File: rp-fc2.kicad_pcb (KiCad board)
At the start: 4 copper layers, 45 x 75 mm, 92 parts, among them CN1 20021521-00010T1LF, J1 USB_C_Receptacle_USB2.0_16P, J2 Conn_01x03, J3 Conn_01x05, J4 Conn_01x05, J5 Conn_01x05, J6 OV7670 Breakout, SW1 SW_Push, SW3 SW_Push, U1 RP2350A-QFN60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

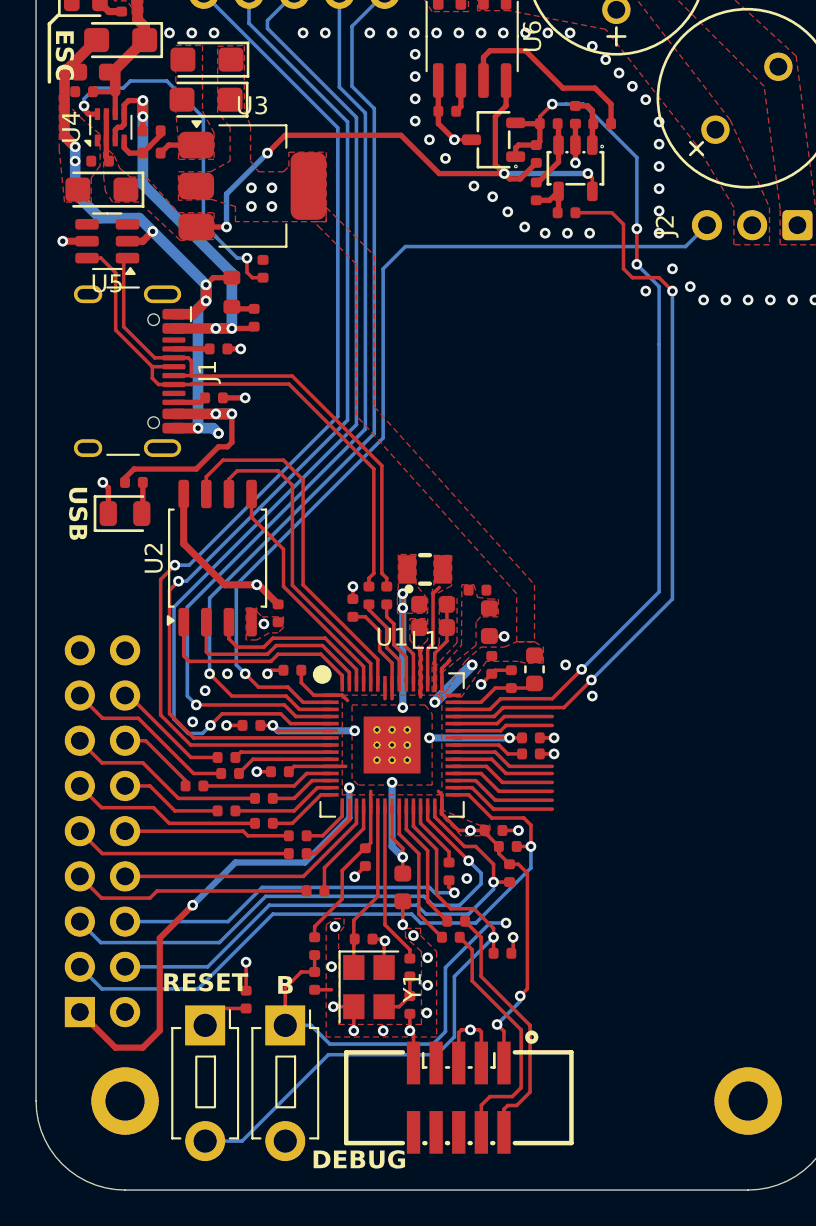
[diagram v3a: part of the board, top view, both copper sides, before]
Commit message: rp2350B -- larger package
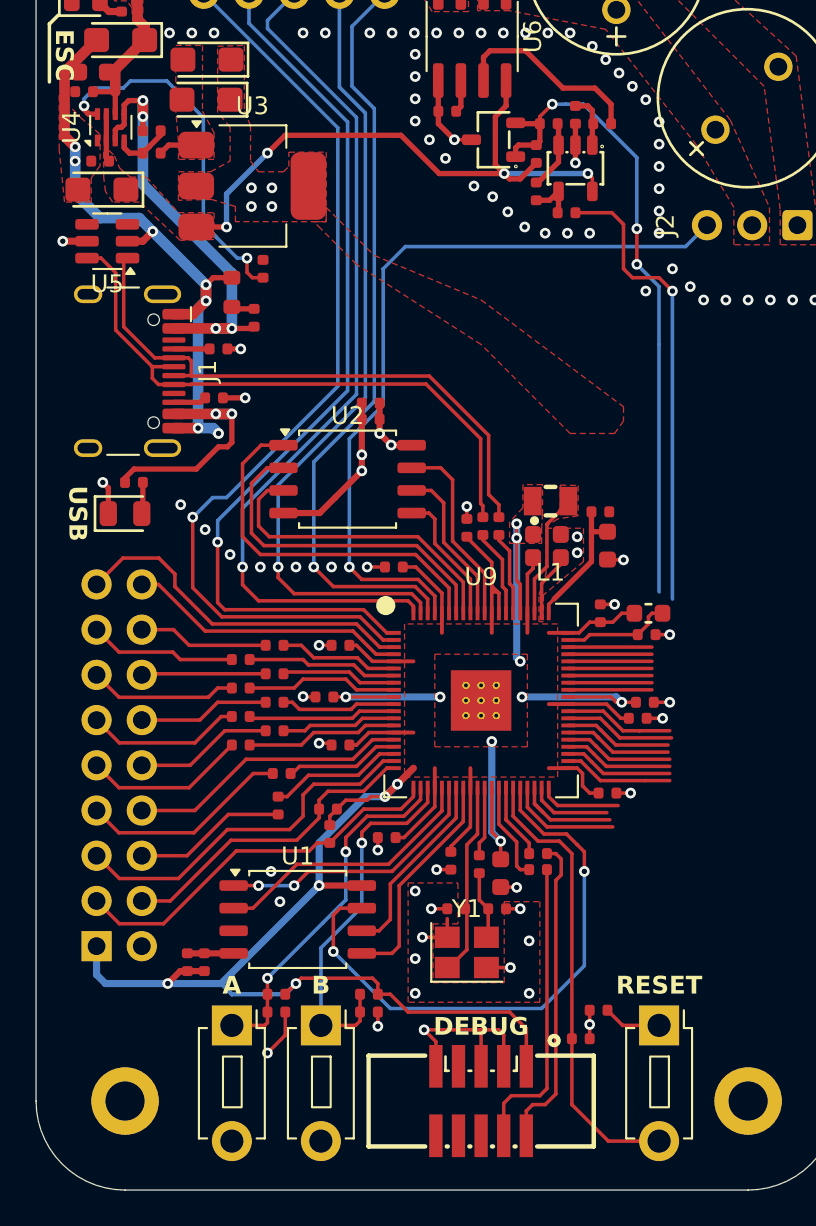
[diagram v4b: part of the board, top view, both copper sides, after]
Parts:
- added C31: 100nF, PCM_JLCPCB:C_0402, F.Cu at (120.1, 115.0)
- added C33: 100nF, PCM_JLCPCB:C_0402, F.Cu at (118.8, 106.7)
- added C34: 100nF, PCM_JLCPCB:C_0402, F.Cu at (131.7, 117.6)
- added C35: 100nF, PCM_JLCPCB:C_0402, F.Cu at (118.7, 140.0)
- added C36: 100nF, PCM_JLCPCB:C_0402, F.Cu at (108.5, 137.2)
- added C37: 100nF, PCM_JLCPCB:C_0402, F.Cu at (109.5, 137.2)
- added R36: 10kΩ, PCM_JLCPCB:R_0402, F.Cu at (118.7, 139.0)
- added SW2: SW_Push, Button_Switch_THT:SW_PUSH_1P1T_6x3.5mm_H4.3_APEM_MJTP1243, F.Cu at (116.0, 140.8)
- added U9: RP2350B-QFN80, RP2350_KiCad:RP2350B_QFN-80_EP_10.573x10.573_Pitch0.4mm, F.Cu at (125.0, 122.5)
- U1: value RP2350A-QFN60 -> W25Q128JVS; footprint RP2350_KiCad:RP2350A_QFN-60_EP_7.75x7.75_Pitch0.4mm -> Package_SO:SOIC-8_5.23x5.23mm_P1.27mm
- moved SW1 25.5 mm to (135.0, 140.8)
- moved C5 22.1 mm to (134.2, 122.6), turned to 0 degrees
- moved R4 19.8 mm to (131.6, 139.9), turned to 0 degrees
- moved C15 12.9 mm to (118.8, 105.8), turned to 180 degrees
- moved C4 11.8 mm to (116.2, 122.3), turned to 180 degrees
- moved U1 11.1 mm to (114.7, 134.8)
- moved R34 10.8 mm to (116.4, 128.6), turned to 180 degrees
- moved R33 10.3 mm to (113.6, 128.4)
- moved R35 10.0 mm to (116.5, 130.0), turned to -90 degrees
- moved C9 8.73 mm to (133.8, 123.5), turned to 0 degrees
- moved U2 8.54 mm to (117.5, 110.1), turned to 0 degrees
- moved R1 8.18 mm to (131.7, 111.9)
- moved L1 8.03 mm to (128.9, 111.3)
- moved C7 8.00 mm to (134.3, 118.8), turned to 0 degrees
- moved C1 7.91 mm to (132.1, 113.8)
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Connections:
- C1 pad 1: Net-(U1-VREG_AVDD) -> Net-(U9-VREG_AVDD)
- C18 pad 1: Net-(U1-RUN) -> Net-(U9-RUN)
- L1 pad 1: Net-(U1-VREG_LX) -> Net-(U9-VREG_LX)
- R1 pad 2: Net-(U1-VREG_AVDD) -> Net-(U9-VREG_AVDD)
- R2 pad 1: Net-(U1-USB_DP) -> Net-(U9-USB_DP)
- R23 pad 1: Net-(U1-GPIO6) -> Net-(U9-GPIO8)
- R25 pad 1: Net-(U1-GPIO7) -> Net-(U9-GPIO9)
- R26 pad 1: Net-(U1-GPIO8) -> Net-(U9-GPIO10)
- R27 pad 1: Net-(U1-GPIO9) -> Net-(U9-GPIO11)
- R28 pad 1: Net-(U1-GPIO10) -> Net-(U9-GPIO12)
- R29 pad 1: Net-(U1-GPIO11) -> Net-(U9-GPIO13)
- R3 pad 1: Net-(U1-USB_DM) -> Net-(U9-USB_DM)
- R30 pad 1: Net-(U1-GPIO12) -> Net-(U9-GPIO14)
- R31 pad 1: Net-(U1-GPIO13) -> Net-(U9-GPIO15)
- R32 pad 1: Net-(U1-GPIO15) -> Net-(U9-GPIO17)
- R33 pad 1: Net-(U1-GPIO16) -> Net-(U9-GPIO18)
- R6 pad 2: Net-(U1-SWCLK) -> Net-(U9-SWCLK)
- R7 pad 2: Net-(U1-SWDIO) -> Net-(U9-SWDIO)
- SW1 pad 2: Net-(U1-RUN) -> Net-(U9-RUN)
- U1 pad 1: +3V3 -> SPI1_CS1
- U1 pad 2: CH1 -> SPI1_MISO
- U1 pad 3: CH6 -> unconnected-(U1-IO2-Pad3)
- U1 pad 4: CH5 -> GND
- U1 pad 5: CH4 -> SPI1_MOSI
- U1 pad 6: +1V1 -> SPI1_SCK
- U1 pad 7: CH3 -> FLASH2_RESET
- U1 pad 8: CH2 -> +3V3
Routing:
- net Net-(U1-RUN): track 33.8 -> 0.00 mm, vias 1 -> 0
- net FLASH2_RESET: track 0.00 -> 32.5 mm, vias 0 -> 2
- net Net-(U9-RUN): track 0.00 -> 25.6 mm
- net +3V3: track 88.2 -> 111.7 mm, vias 12 -> 11
- net USR_SW2: track 0.00 -> 20.8 mm, vias 0 -> 1
- net CAMERA_RST: track 0.00 -> 19.8 mm
- net GND: track 81.9 -> 98.5 mm, vias 93 -> 100
- net CAMERA_PWDN: track 0.00 -> 15.8 mm
- net SIO_C: track 37.4 -> 21.8 mm, vias 1 -> 0
- net SPI1_MISO: track 0.00 -> 15.3 mm
- net SPI1_CS1: track 0.00 -> 15.3 mm, vias 0 -> 2
- net I_COND: track 41.1 -> 26.0 mm, vias 2 -> 1
- net I_COND_2_5: track 51.0 -> 36.7 mm, vias 4 -> 3
- net SPI1_MOSI: track 0.00 -> 12.7 mm
- net SIO_D: track 30.2 -> 17.8 mm, vias 1 -> 0
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- added copper zone on F.Cu, net Net-(U9-VREG_LX)
- removed copper zone on F.Cu, net Net-(U1-VREG_AVDD)
- removed copper zone on F.Cu, net Net-(U1-VREG_LX)
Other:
- board text added: "A"

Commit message: nrf52833-discrete
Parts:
- added AE1: 2.4GHz, PCM_JLCPCB:L_1206, F.Cu at (95.0, 138.6)
- added C38: 100nF, PCM_JLCPCB:C_0402, F.Cu at (138.0, 137.4)
- added C39: 4.7uF, PCM_JLCPCB:C_0603, F.Cu at (132.4, 136.6)
- added C40: 1uF, PCM_JLCPCB:C_0402, F.Cu at (140.8, 140.5)
- added C41: 100nF, PCM_JLCPCB:C_0402, F.Cu at (139.1, 144.8)
- added C42: 1uF, PCM_JLCPCB:C_0402, F.Cu at (139.8, 140.5)
- added C43: 100pF, PCM_JLCPCB:C_0402, F.Cu at (136.8, 147.5)
- added C44: 100nF, PCM_JLCPCB:C_0402, F.Cu at (129.7, 143.4)
- added C45: 1nF, PCM_JLCPCB:C_0402, F.Cu at (130.5, 145.3)
- added C46: 100nF, PCM_JLCPCB:C_0402, F.Cu at (155.7, 144.1)
- added C47: 1pF, PCM_JLCPCB:C_0402, F.Cu at (133.7, 147.2)
- added C48: 1.2pF, PCM_JLCPCB:C_0402, F.Cu at (133.7, 150.9)
- added C49: 15pF, PCM_JLCPCB:C_0402, F.Cu at (139.9, 146.7)
- added C50: 15pF, PCM_JLCPCB:C_0402, F.Cu at (142.0, 146.7)
- added CN2: 20021521-00010T1LF, easyeda2kicad:IDC-SMD_10P-P1.27_X1270WVS-2X05B-6TV01, F.Cu at (114.2, 155.4)
- added D3: H5VUT1B, PCM_JLCPCB:SOT-143-4_L2.9-W1.3-P1.90-LS2.4-BL-1, F.Cu at (163.9, 124.1)
- added J7: U.FL, PCM_JLCPCB:IPEX-SMD_BWIPX-1-001E, F.Cu at (133.2, 154.8)
- added J8: Conn_01x04, Connector_PinHeader_2.54mm:PinHeader_1x04_P2.54mm_Vertical, F.Cu at (170.4, 119.8)
- added L2: 4.7nH,300mA, PCM_JLCPCB:L_0402, F.Cu at (133.2, 149.0)
- added L3: 2.2nH,300mA, PCM_JLCPCB:L_0402, F.Cu at (133.2, 152.4)
- added R37: 10kΩ, PCM_JLCPCB:R_0402, F.Cu at (155.7, 146.0)
- added R38: 10kΩ, PCM_JLCPCB:R_0402, F.Cu at (130.6, 136.4)
- added R39: 10kΩ, PCM_JLCPCB:R_0402, F.Cu at (130.6, 139.2)
- added R40: 10kΩ, PCM_JLCPCB:R_0402, F.Cu at (128.6, 142.0)
- added SW4: SW_Push, Button_Switch_THT:SW_PUSH_1P1T_6x3.5mm_H4.3_APEM_MJTP1243, F.Cu at (156.7, 141.6)
- added U10: nRF52833_QDxx, Package_DFN_QFN:QFN-40-1EP_5x5mm_P0.4mm_EP3.6x3.6mm, F.Cu at (135.0, 142.0)
- added X1: X201632MOB4SI, PCM_JLCPCB:OSC-SMD_4P-L3.2-W2.5-BL, F.Cu at (140.4, 148.9)
- moved SW1 27.8 mm to (109.0, 150.6), turned to 180 degrees
- moved R4 22.1 mm to (111.3, 148.6), turned to 180 degrees
- moved C18 20.2 mm to (111.3, 147.6)
- moved H4 11.2 mm to (145.0, 155.0)
- moved H3 10.0 mm to (105.0, 155.0)
- moved SW2 8.47 mm to (109.0, 145.6), turned to 180 degrees
- moved R36 7.52 mm to (112.4, 143.1), turned to -90 degrees
- moved CN1 7.41 mm to (117.6, 144.6), turned to 90 degrees
- moved C35 6.91 mm to (112.0, 141.7), turned to 180 degrees
- moved R24 5.66 mm to (110.2, 143.6)
- moved H2 5.00 mm to (145.0, 80.0)
- moved C32 4.20 mm to (110.2, 142.6)
- moved SW3 2.06 mm to (109.0, 140.6), turned to 180 degrees
- moved R6 0.95 mm to (127.9, 132.9), turned to 90 degrees
- moved R1 0.72 mm to (131.0, 111.8), turned to -90 degrees
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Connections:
- C18 pad 1: Net-(U9-RUN) -> RP2350_RUN
- CN1 pad 10: unconnected-(CN1-Pad10) -> RP2350_RUN
- SW1 pad 2: Net-(U9-RUN) -> RP2350_RUN
- U9 pad 35: Net-(U9-RUN) -> RP2350_RUN
- U9 pad 37: unconnected-(U9-GPIO29-Pad37) -> NRF_AUX1
- U9 pad 38: unconnected-(U9-GPIO30-Pad38) -> NRF_AUX2
- U9 pad 39: unconnected-(U9-GPIO31-Pad39) -> NRF_AUX3
- U9 pad 40: unconnected-(U9-GPIO32-Pad40) -> SPI0_MISO
- U9 pad 42: unconnected-(U9-GPIO33-Pad42) -> SPI0_CS
- U9 pad 43: unconnected-(U9-GPIO34-Pad43) -> SPIO_SCK
- U9 pad 44: unconnected-(U9-GPIO35-Pad44) -> SPIO_MOSI
- U9 pad 57: unconnected-(U9-GPIO46_ADC6-Pad57) -> I_COND
- U9 pad 58: unconnected-(U9-GPIO47_ADC7-Pad58) -> I_COND_2_5
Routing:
- net +3V3: track 111.7 -> 229.7 mm, vias 11 -> 18
- net RP2350_RUN: track 0.00 -> 45.7 mm, vias 0 -> 2
- net GND: track 98.5 -> 127.2 mm, vias 100 -> 171
- net NRF_SWCLK: track 0.00 -> 28.6 mm
- net NRF_NRESET: track 0.00 -> 28.5 mm, vias 0 -> 2
- net Net-(U9-RUN): track 25.6 -> 0.00 mm
- net NRF_SWDIO: track 0.00 -> 24.3 mm
- net NRF_AUX1: track 0.00 -> 21.4 mm
- net NRF_AUX2: track 0.00 -> 19.9 mm
- net NRF_AUX3: track 0.00 -> 18.2 mm
- net SPIO_MOSI: track 0.00 -> 18.1 mm
- net SPIO_SCK: track 0.00 -> 17.4 mm
- net SPI0_CS: track 0.00 -> 16.6 mm
- net SPI0_MISO: track 0.00 -> 15.1 mm
- net /IO/DEC4_6: track 0.00 -> 12.6 mm, vias 0 -> 2
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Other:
- board size 45 x 75 mm -> 50 x 85 mm
- board text added: "NRF DEBUG"
- board text added: "PI DEBUG"
- board text added: "PI RUN"
- board text removed: "DEBUG"
- board text removed: "RESET"

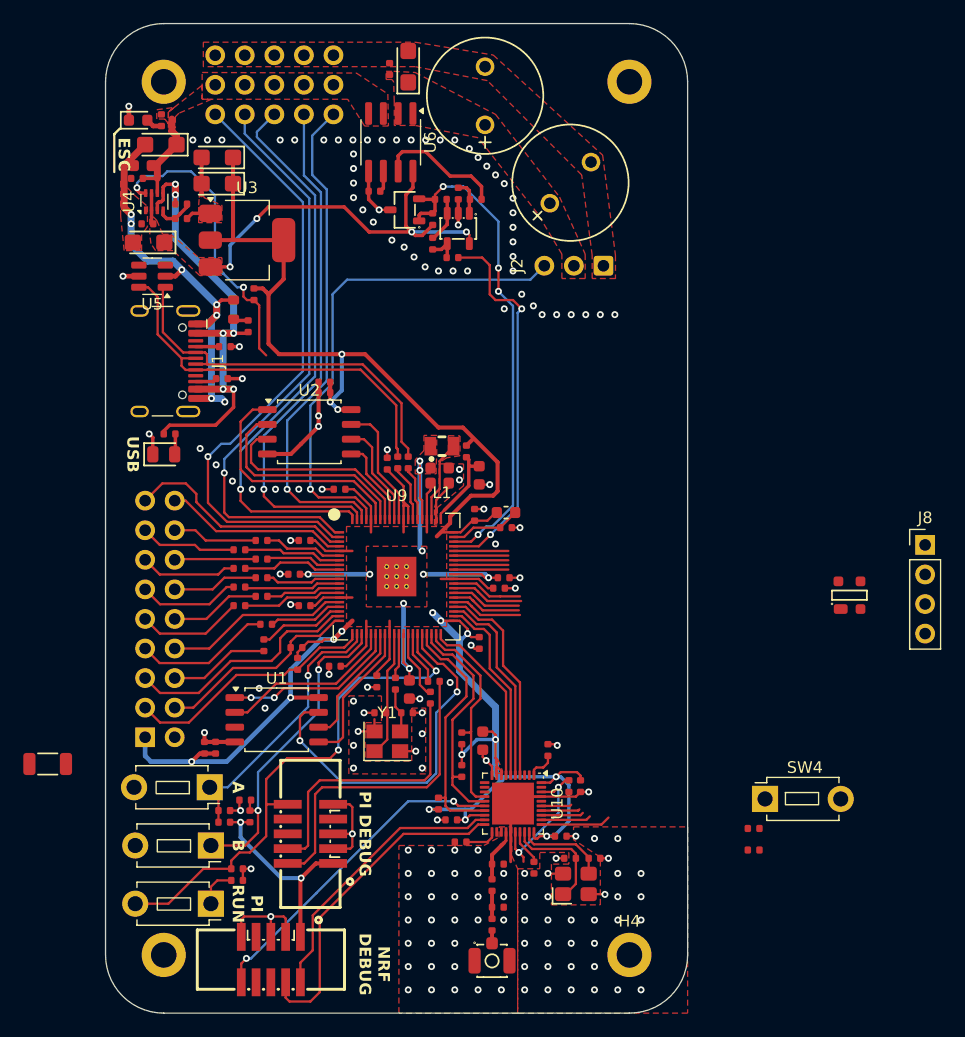
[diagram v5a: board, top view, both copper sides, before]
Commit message: nrf54L BLE module
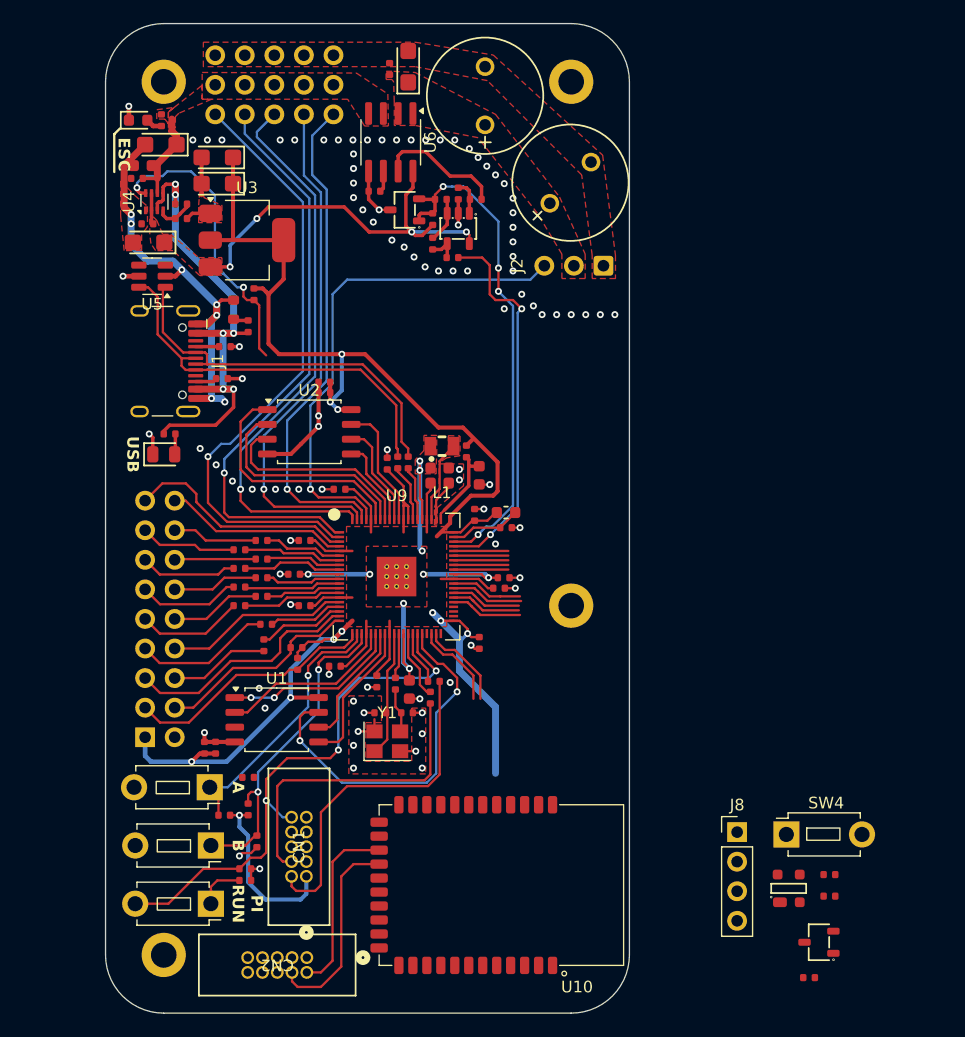
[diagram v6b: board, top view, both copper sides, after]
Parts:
- removed AE1: 2.4GHz, PCM_JLCPCB:L_1206
- removed C38, C41, C44: 100nF, PCM_JLCPCB:C_0402
- removed C39: 4.7uF, PCM_JLCPCB:C_0603
- removed C40, C42: 1uF, PCM_JLCPCB:C_0402
- removed C43: 100pF, PCM_JLCPCB:C_0402
- removed C45: 1nF, PCM_JLCPCB:C_0402
- removed C47: 1pF, PCM_JLCPCB:C_0402
- removed C48: 1.2pF, PCM_JLCPCB:C_0402
- removed C49, C50: 15pF, PCM_JLCPCB:C_0402
- removed J7: U.FL, PCM_JLCPCB:IPEX-SMD_BWIPX-1-001E
- removed L2: 4.7nH,300mA, PCM_JLCPCB:L_0402
- removed L3: 2.2nH,300mA, PCM_JLCPCB:L_0402
- removed R39, R40: 10kΩ, PCM_JLCPCB:R_0402
- removed X1: X201632MOB4SI, PCM_JLCPCB:OSC-SMD_4P-L3.2-W2.5-BL
- added U11: CJ431, PCM_JLCPCB:SOT-23-3_L2.9-W1.6-P1.90-LS2.8-BR, F.Cu at (161.3, 153.9)
- CN1, CN2: footprint easyeda2kicad:IDC-SMD_10P-P1.27_X1270WVS-2X05B-6TV01 -> DigiKey:CONN_3220-10-0100-00_CNC
- R38: value 10kΩ -> 1kΩ
- U10: value nRF52833_QDxx -> MK19; footprint Package_DFN_QFN:QFN-40-1EP_5x5mm_P0.4mm_EP3.6x3.6mm -> RF_Module:MokoSmart MK19
- moved R38 36.2 mm to (160.4, 156.9), turned to 0 degrees
- moved H4 30.4 mm to (140.0, 125.0)
- moved J8 29.5 mm to (154.2, 144.4)
- moved D3 25.7 mm to (158.7, 149.3)
- moved C46 7.62 mm to (162.2, 148.1)
- moved R37 7.62 mm to (162.2, 149.9)
- moved U10 7.07 mm to (134.0, 149.0)
- moved H2 5.00 mm to (140.0, 80.0)
- moved C35 3.69 mm to (113.0, 145.2), turned to -90 degrees
- moved CN1 3.67 mm to (117.2, 148.2)
- moved SW4 3.56 mm to (158.5, 144.7)
- moved C32 3.51 mm to (112.2, 139.8)
- moved CN2 3.09 mm to (117.3, 155.2)
- moved C18 0.70 mm to (112.0, 147.6)
- moved R4 0.70 mm to (112.0, 148.6)
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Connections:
- R38 pad 1: NRF_AUX3 -> Net-(U10-P1.08/CLK16M/EXTREF)
- U10 pad 1: /IO/DEC1 -> unconnected-(U10-P0.03/GRTCPWM-Pad1)
- U10 pad 14: NRF_AUX3 -> unconnected-(U10-P1.05/RADIO6/AIN1-Pad14)
- U10 pad 15: NRF_AUX2 -> unconnected-(U10-P1.06/AIN2-Pad15)
- U10 pad 16: NRF_NRESET -> unconnected-(U10-P1.07/AIN3-Pad16)
- U10 pad 17: NRF_AUX1 -> Net-(U10-P1.08/CLK16M/EXTREF)
- U10 pad 18: +3V3 -> unconnected-(U10-P2.00-Pad18)
- U10 pad 19: NRF_SWDIO -> NRF_SWCLK
- U10 pad 20: NRF_SWCLK -> NRF_SWDIO
- U10 pad 21: /IO/DEC5 -> unconnected-(U10-P2.01-Pad21)
- U10 pad 24: /IO/ANT -> unconnected-(U10-P2.04-Pad24)
- U10 pad 25: GND -> unconnected-(U10-P2.05-Pad25)
- U10 pad 26: /IO/DEC4_6 -> unconnected-(U10-P2.06/TRACECLK-Pad26)
- U10 pad 27: /IO/DEC3 -> unconnected-(U10-P2.07/TRACEDATA0/SWO-Pad27)
- U10 pad 28: Net-(U10-XC1) -> unconnected-(U10-P2.08-Pad28)
- U10 pad 29: Net-(U10-XC2) -> unconnected-(U10-P2.09-Pad29)
- U10 pad 30: +3V3 -> unconnected-(U10-P2.10-Pad30)
- U10 pad 33: unconnected-(U10-AIN4/P0.28-Pad33) -> NRF_NRESET
- U10 pad 4: SPIO_MOSI -> unconnected-(U10-P1.10/RADIO1-Pad4)
- U10 pad 5: SPIO_SCK -> unconnected-(U10-P1.11/RADIO2/AIN4-Pad5)
- U10 pad 6: SPI0_CS -> unconnected-(U10-P1.12/RADIO3/AIN5-Pad6)
- U10 pad 7: SPI0_MISO -> unconnected-(U10-P1.13/RADIO4/AIN6-Pad7)
- U10 pad 8: +3V3 -> unconnected-(U10-P1.14/RADIO5/AIN7-Pad8)
- U10 pad 9: +3V3 -> unconnected-(U10-VDD-Pad9)
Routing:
- net +3V3: track 229.7 -> 185.1 mm, vias 18 -> 11
- net GND: track 127.2 -> 90.1 mm, vias 171 -> 101
- net NRF_NRESET: track 28.5 -> 0.00 mm, vias 2 -> 0
- net NRF_AUX1: track 21.4 -> 0.00 mm
- net SPIO_MOSI: track 18.1 -> 0.00 mm
- net SPIO_SCK: track 17.4 -> 0.00 mm
- net SPI0_CS: track 16.6 -> 0.00 mm
- net SPI0_MISO: track 15.1 -> 0.00 mm
- net /IO/DEC4_6: track 12.6 -> 0.00 mm, vias 2 -> 0
- net NRF_AUX2: track 19.9 -> 7.56 mm
- net NRF_SWCLK: track 28.6 -> 17.4 mm
- net NRF_AUX3: track 18.2 -> 7.67 mm
- net Net-(U10-XC1): track 9.72 -> 0.00 mm
- net NRF_SWDIO: track 24.3 -> 15.5 mm
- net Net-(U10-XC2): track 7.80 -> 0.00 mm
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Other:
- board size 50 x 85 mm -> 45 x 85 mm
- board text removed: "NRF DEBUG"
- board text removed: "PI DEBUG"
